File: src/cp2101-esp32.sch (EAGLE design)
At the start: 4 parts

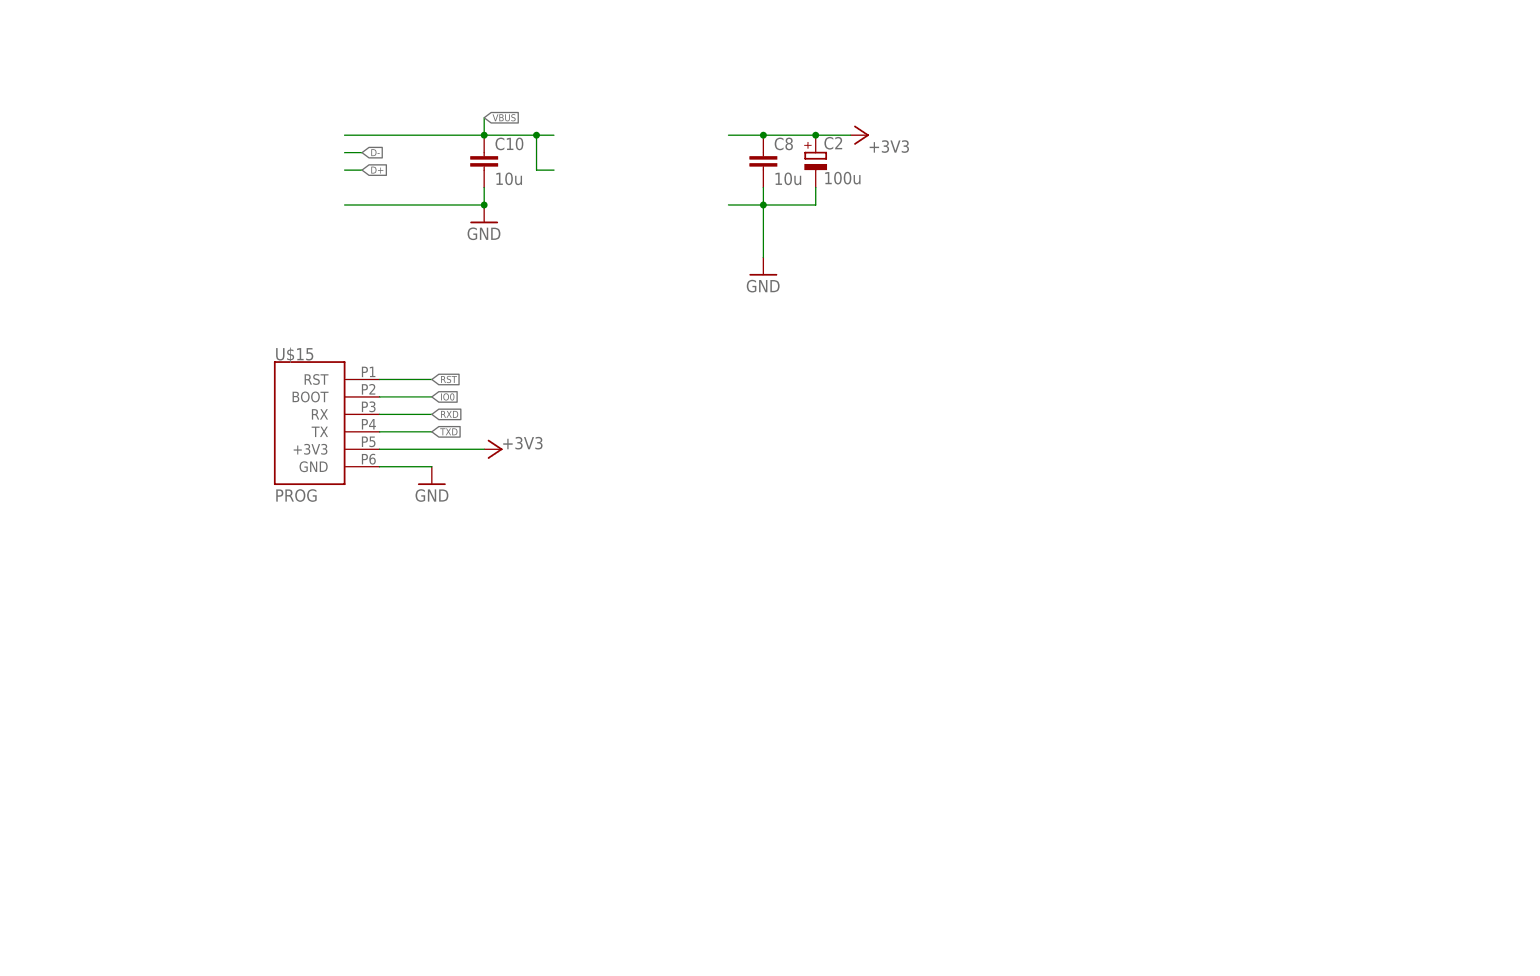
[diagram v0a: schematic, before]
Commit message: Added connectors
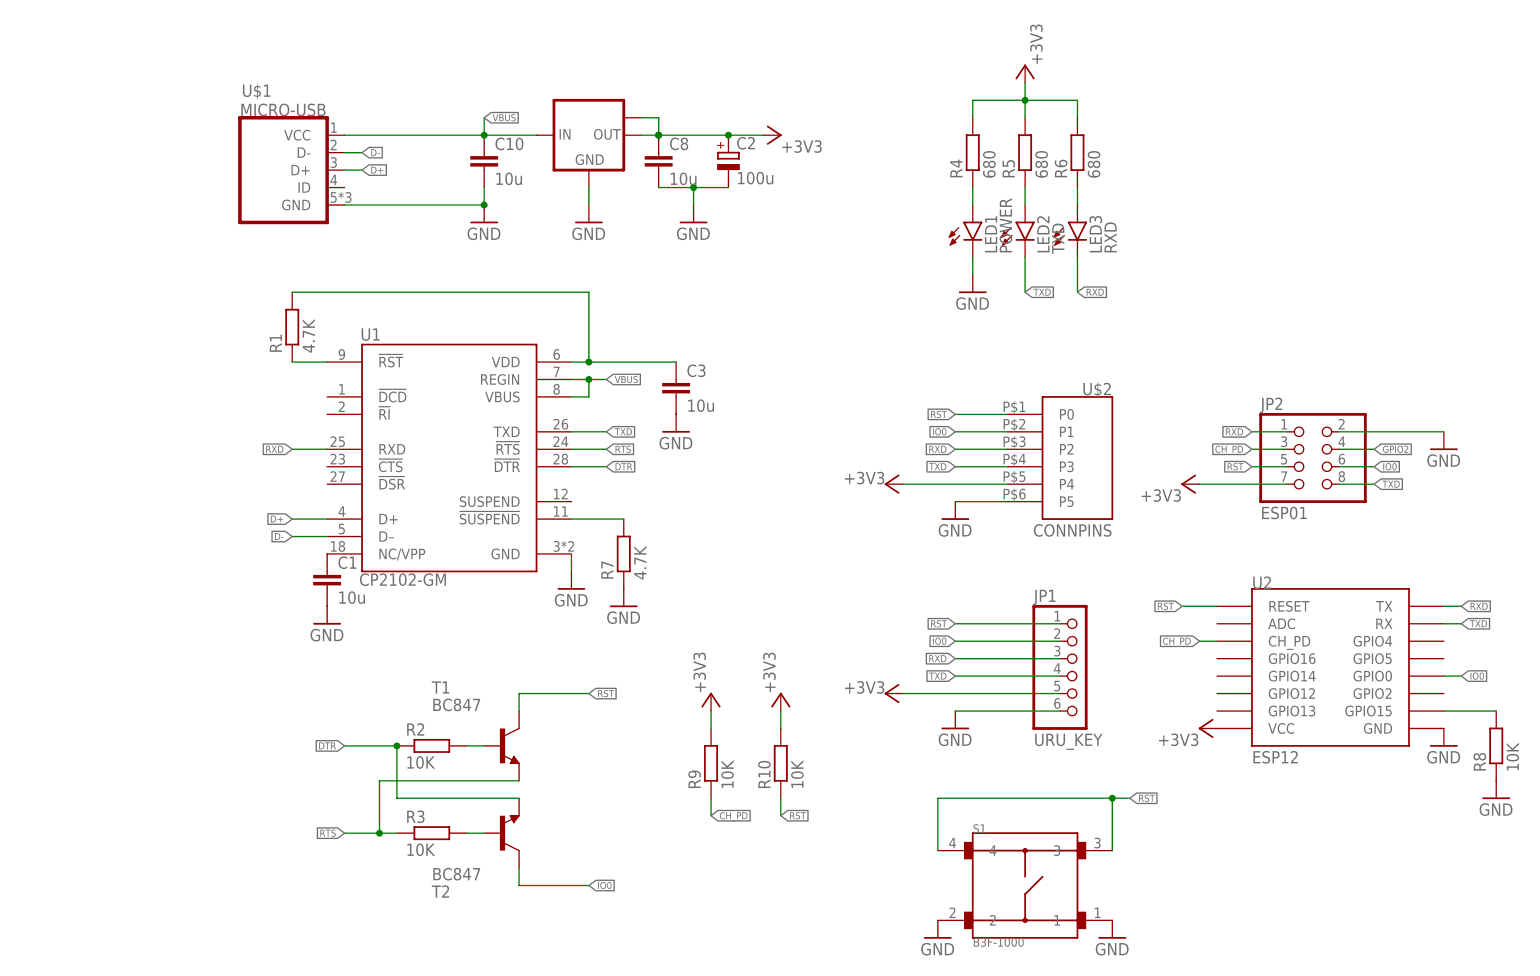
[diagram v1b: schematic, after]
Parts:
- removed U$15: PROG, pads:PROG
- added C1, C3: 10u, rcl:C-EUC0805
- added IC1: LM1117MPX-3.3, lm1117:LM1117MPX-3.3
- added JP1: URU_KEY, pinhead:PINHD-1X6/90
- added JP2: ESP01, pinhead:PINHD-2X4
- added LED1: POWER, led:LEDCHIP-LED0805
- added LED2: TXD, led:LEDCHIP-LED0805
- added LED3: RXD, led:LEDCHIP-LED0805
- added R1, R7: 4.7K, rcl:R-EU_R0805
- added R10, R2, R3, R8, R9: 10K, rcl:R-EU_R0805
- added R4, R5, R6: 680, rcl:R-EU_R0805
- added S1: B3F-1000, B3F-1000:B3F-1000
- added T1, T2: BC847, transistor:BC847
- added U$1: MICRO-USB, microusb:MICRO-USB
- added U$2: CONNPINS, CONN:CONNPINS
- added U1: CP2102-GM, CP2102-GM:CP2102-GM
- added U2: ESP12, esp8266modules:ESP12
- C10, C8: device rcl:C-EUC0603 -> rcl:C-EUC0805
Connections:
- new net CH_PD: JP2.3, R9.1, U2.CH_PD
- new net D+: U$1.D+, U1.D+
- new net D-: U$1.D-, U1.D–
- new net DTR: R2.1, T2.E, U1.!DTR
- new net GPIO2: JP2.4
- new net N$1: C1.1, U1.NC/VPP
- new net N$10: LED2.A, R5.1
- new net N$11: LED3.A, R6.1
- new net N$2: C3.1, R1.2, U1.VDD
- new net N$3: R7.2, U1.!SUSPEND
- new net N$4: R8.2, U2.GPIO15
- new net N$6: LED1.A, R4.1
- new net N$7: R1.1, U1.!RST
- new net N$8: R2.2, T1.B
- new net N$9: R3.2, T2.B
- new net RTS: R3.1, T1.E, U1.!RTS
- net +3V3: now also IC1.OUT, IC1.OUT1, JP1.5, JP2.7, R10.2, R4.2, R5.2, R6.2, R9.2, U$2.P4, U2.VCC; no longer U$15.+3V3
- net GND: now also C1.2, C3.2, IC1.GND, JP1.6, JP2.2, LED1.C, R7.1, R8.1, S1.1, S1.2, U$1.GND, U$2.P5, U1.GND, U2.GND; no longer U$15.GND
- net IO0: now also JP1.2, JP2.6, T2.C, U$2.P1, U2.GPIO0; no longer U$15.BOOT
- net RST: now also JP1.1, JP2.5, R10.1, S1.3, S1.4, T1.C, U$2.P0, U2.RESET; no longer U$15.RST
- net RXD: now also JP1.3, JP2.1, LED3.C, U$2.P2, U1.RXD, U2.TX; no longer U$15.RX
- net TXD: now also JP1.4, JP2.8, LED2.C, U$2.P3, U1.TXD, U2.RX; no longer U$15.TX
- net VBUS: now also IC1.IN, U$1.VCC, U1.REGIN, U1.VBUS
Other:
- moved on the sheet: C2, C8

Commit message: USB TypeC connector; Smaller board
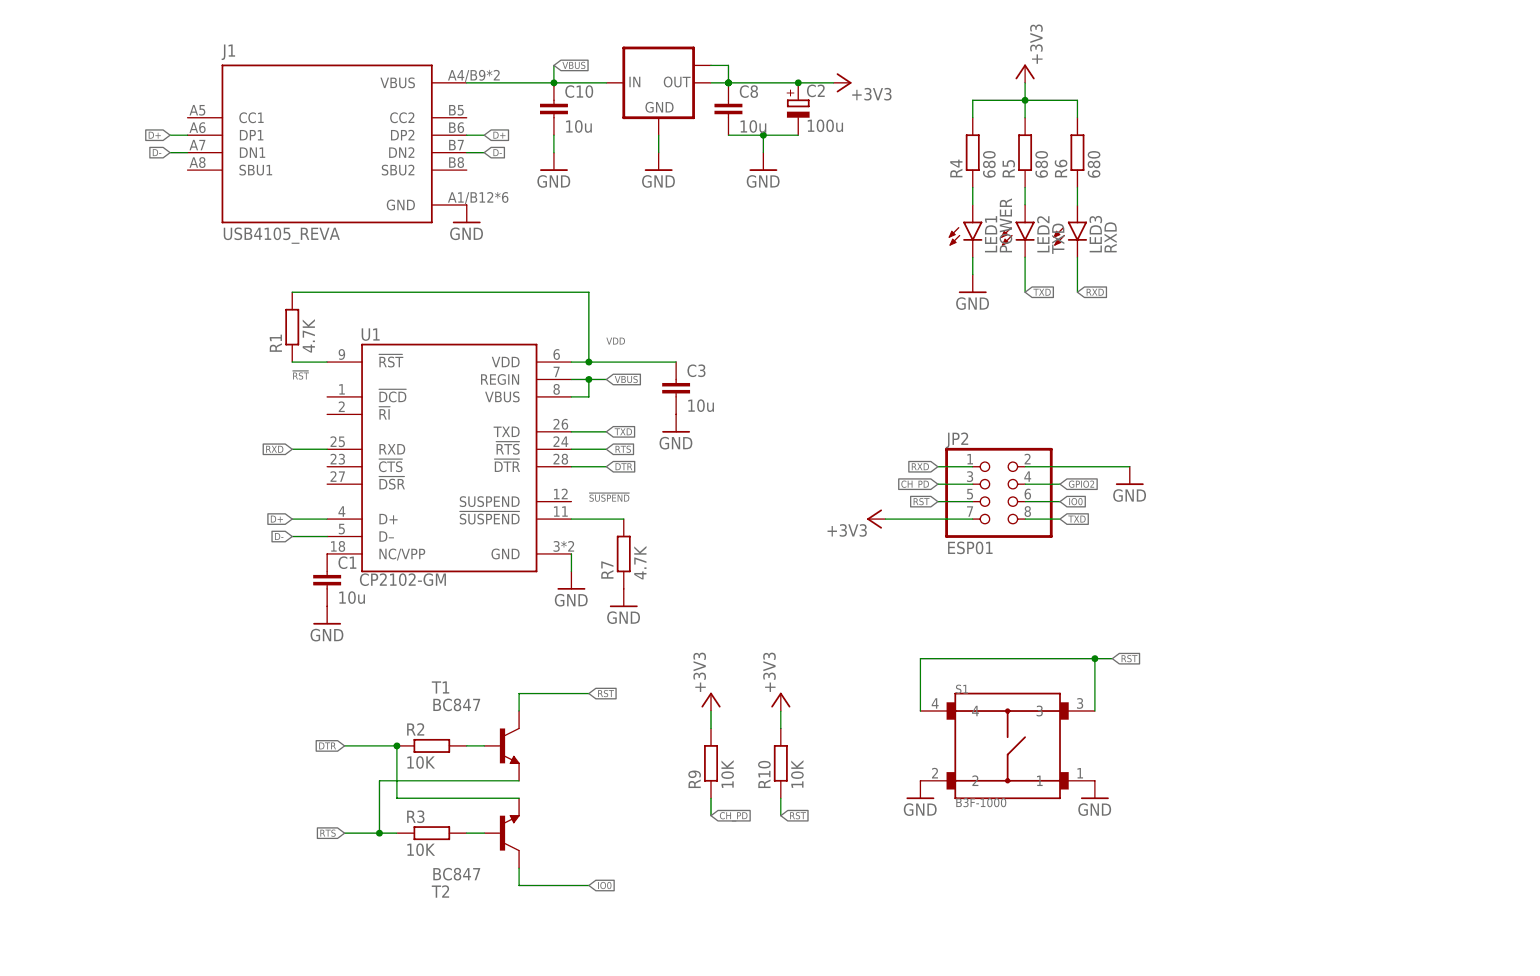
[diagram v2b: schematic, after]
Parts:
- removed JP1: URU_KEY, pinhead:PINHD-1X6/90
- removed R8: 10K, rcl:R-EU_R0805
- removed U$1: MICRO-USB, microusb:MICRO-USB
- removed U$2: CONNPINS, CONN:CONNPINS
- removed U2: ESP12, esp8266modules:ESP12
- added J1: USB4105_REVA, USB4105_REVA:USB4105_REVA
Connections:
- net N$2 renamed VDD
- net N$3 renamed !SUSPEND
- net N$7 renamed !RST
- removed net N$4: R8.2, U2.GPIO15
- net +3V3: no longer JP1.5, U$2.P4, U2.VCC
- net CH_PD: no longer U2.CH_PD
- net D+: now also J1.DP1, J1.DP2; no longer U$1.D+
- net D-: now also J1.DN1, J1.DN2; no longer U$1.D-
- net GND: now also J1.GND; no longer JP1.6, R8.1, U$1.GND, U$2.P5, U2.GND
- net IO0: no longer JP1.2, U$2.P1, U2.GPIO0
- net RST: no longer JP1.1, U$2.P0, U2.RESET
- net RXD: no longer JP1.3, U$2.P2, U2.TX
- net TXD: no longer JP1.4, U$2.P3, U2.RX
- net VBUS: now also J1.VBUS; no longer U$1.VCC
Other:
- moved on the sheet: C10, C2, C8, JP2, S1

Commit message: .
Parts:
- removed C3: 10u, rcl:C-EUC0805
- removed R1, R7: 4.7K, rcl:R-EU_R0805
- removed S1: B3F-1000, B3F-1000:B3F-1000
- added R8: 10K, rcl:R-EU_R0805
- added U$1: SWITCH2X4-MICRO, SMD Tact:SWITCH2X4-MICRO
- U1: value CP2102-GM -> CP2104-F03-GM; device CP2102-GM:CP2102-GM -> CP2104:CP2104-F03-GM
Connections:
- removed net !RST: R1.1, U1.!RST
- removed net !SUSPEND: R7.2, U1.!SUSPEND
- removed net VDD: C3.1, R1.2, U1.VDD
- new net N$7: C1.1, U1.VPP
- net +3V3: now also R8.2, U1.REGIN, U1.VDD, U1.VIO
- net D+: now also U1.DP; no longer U1.D+
- net D-: now also U1.DN; no longer U1.D–
- net GND: now also U$1.P$2; no longer C3.2, R7.1, S1.1, S1.2
- net N$1: now also R8.1, U1.!RST!; no longer C1.1, U1.NC/VPP
- net RST: now also U$1.P$1; no longer S1.3, S1.4
- net VBUS: no longer U1.REGIN, U1.VBUS
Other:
- moved on the sheet: C1
